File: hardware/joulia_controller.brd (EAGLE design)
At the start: 122.9 x 67.9 mm, 41 parts, among them IC1 LM2902D, IC2 LM2902D, U1 MMBT2222ALT1G, U2 MMBT2222ALT1G

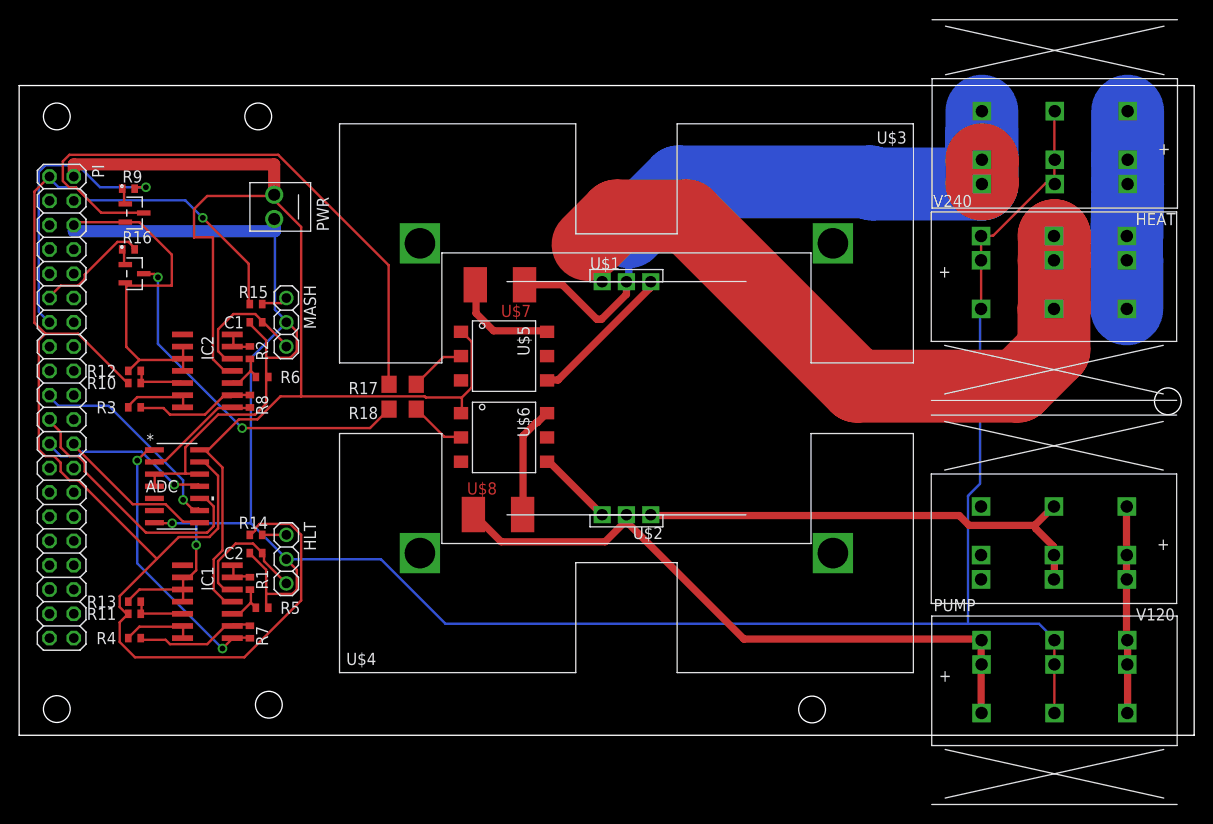
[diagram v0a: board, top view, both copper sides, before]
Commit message: Complete wiring with HV circuit and rearrangement
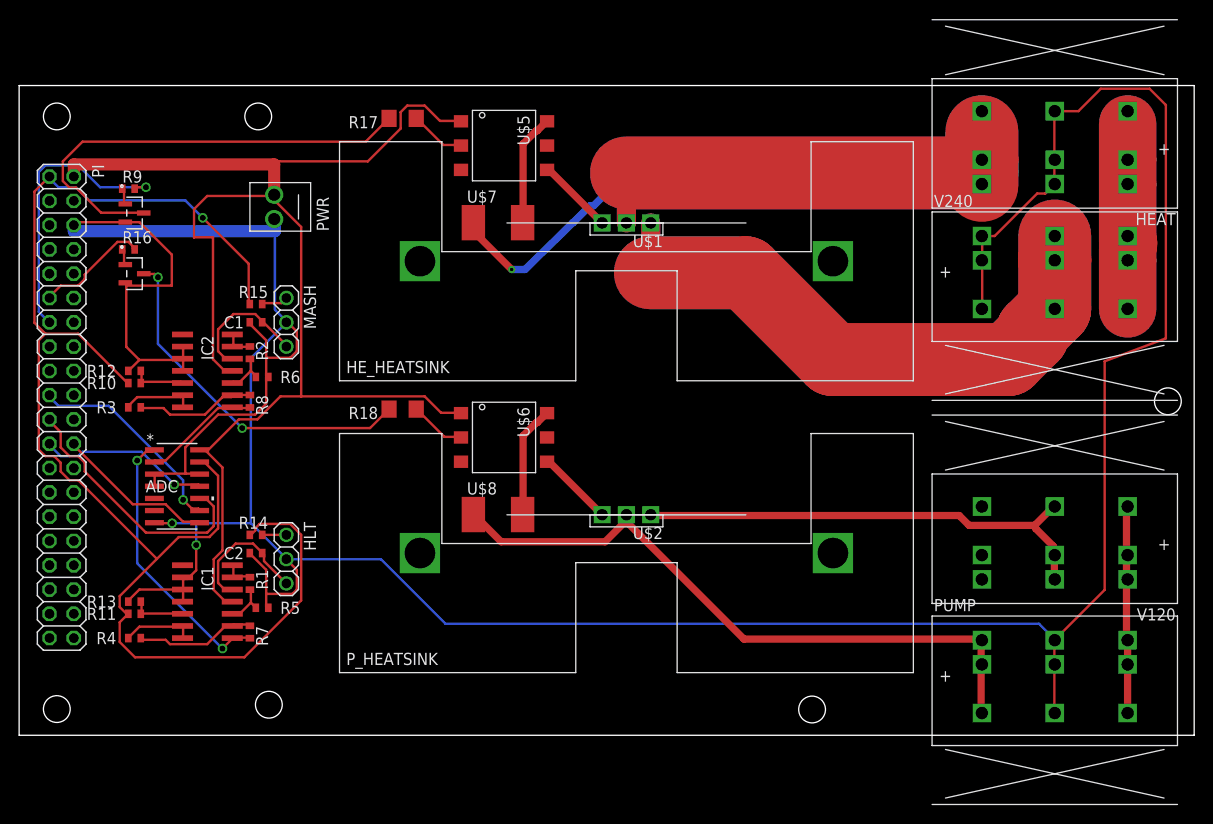
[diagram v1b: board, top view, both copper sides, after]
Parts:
- removed U$3: VM1-038-1AE, digikey:VM1-038-1AE
- added HE_HEATSINK: VM1-038-1AE, digikey:VM1-038-1AE
- moved R17 27.8 mm to (40.1, 64.5)
- moved U$5 22.0 mm to (50.7, 61.7)
- moved U$7 6.49 mm to (50.1, 53.6), turned to 0 degrees
- moved U$1 6.15 mm to (63.5, 53.6), turned to 180 degrees
- moved V120 0.08 mm to (108.3, 16.3)
- moved V240 0.08 mm to (108.3, 52.2)
- renumbered U$4 to P_HEATSINK
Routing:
- net N$22: track 74.7 -> 125.6 mm, vias 0 -> 1
- net N$32: track 75.5 -> 122.9 mm
- net GND: track 325.1 -> 367.4 mm
- net N$29: track 20.8 -> 43.8 mm
- net N$13: track 63.5 -> 47.9 mm
- net +5V: track 135.2 -> 150.0 mm
- net N$19: track 15.5 -> 8.06 mm

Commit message: Fix board size and hole placement.
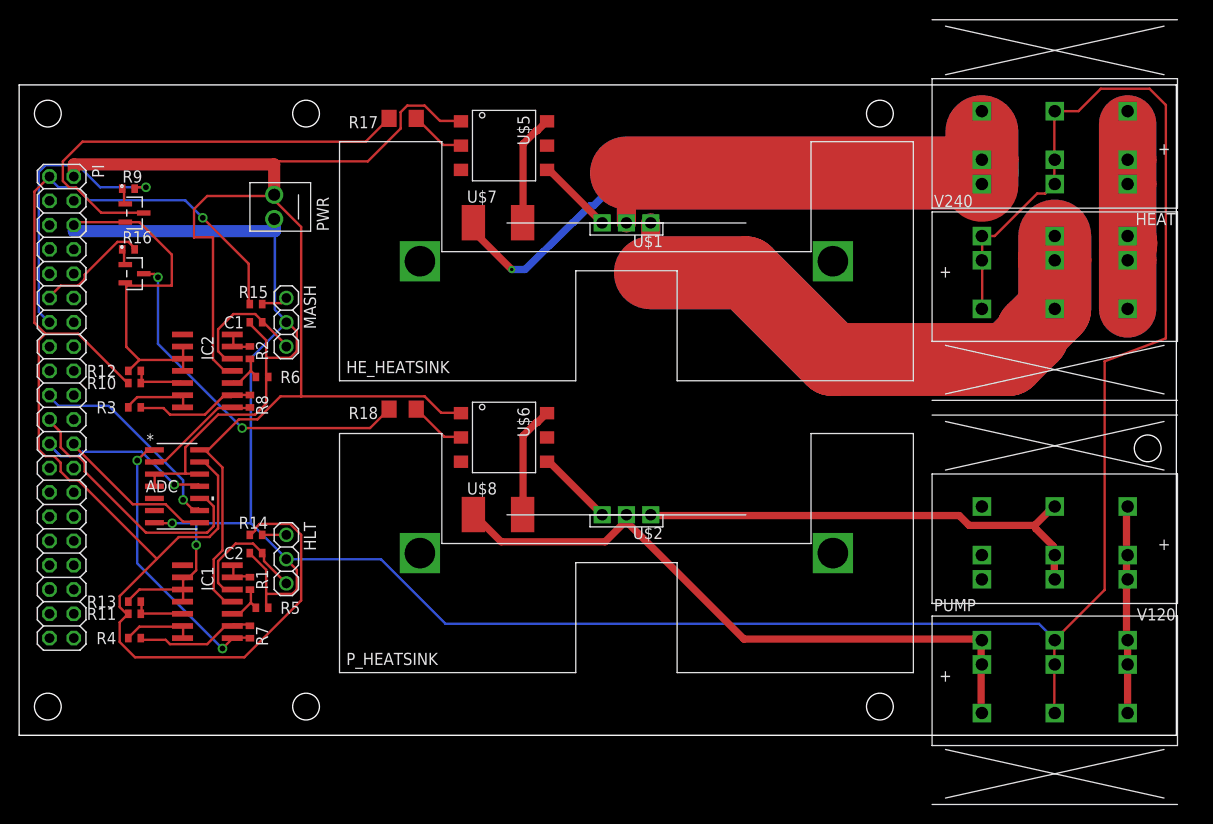
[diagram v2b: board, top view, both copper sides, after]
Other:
- board size 122.9 x 67.9 mm -> 121 x 68 mm
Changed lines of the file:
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@@
 <board>
 <plain>
-<wire x1="0" y1="0" x2="122.86" y2="0" width="0" layer="20"/>
-<wire x1="122.86" y1="0" x2="122.86" y2="67.935" width="0" layer="20"/>
-<wire x1="122.86" y1="67.935" x2="0" y2="67.935" width="0" layer="20"/>
-<wire x1="0" y1="67.935" x2="0" y2="0" width="0" layer="20"/>
-<hole x="3.94" y="64.705" drill="2.8"/>
-<hole x="82.91" y="2.695" drill="2.8"/>
-<hole x="3.94" y="2.74" drill="2.8"/>
-<hole x="120.11" y="34.92" drill="2.8"/>
+<wire x1="0" y1="0" x2="121" y2="0" width="0" layer="20"/>
+<wire x1="121" y1="0" x2="121" y2="68" width="0" layer="20"/>
+<wire x1="121" y1="68" x2="0" y2="68" width="0" layer="20"/>
+<wire x1="0" y1="68" x2="0" y2="0" width="0" layer="20"/>
+<hole x="3" y="65" drill="2.8"/>
+<hole x="90" y="3" drill="2.8"/>
+<hole x="3" y="3" drill="2.8"/>
+<hole x="118" y="30" drill="2.8"/>
 <text x="28.575" y="9.525" size="1.778" layer="26" rot="MR90">JOULIA HOMEBREW CONTROLLER</text>
 <text x="19.05" y="9.525" size="1.778" layer="26" rot="MR90">WILLIAM SCHMITT
 COPYRIGHT, 2017</text>
-<hole x="25" y="64.705" drill="2.8"/>
-<hole x="26.11" y="3.195" drill="2.8"/>
+<hole x="30" y="65" drill="2.8"/>
+<hole x="30" y="3" drill="2.8"/>
+<hole x="90" y="65" drill="2.8"/>
 </plain>
 <attributes>

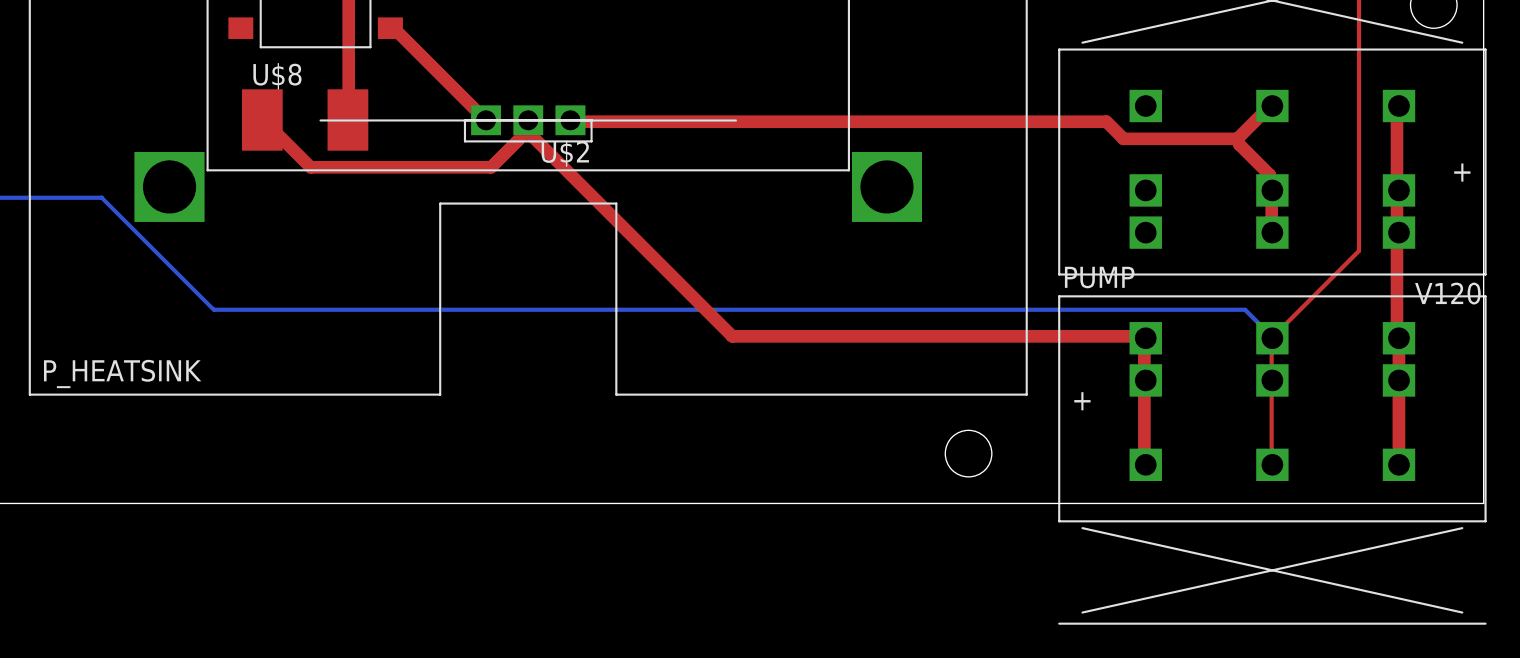
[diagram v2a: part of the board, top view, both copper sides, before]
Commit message: Adjust plugs to be consistently spaced.
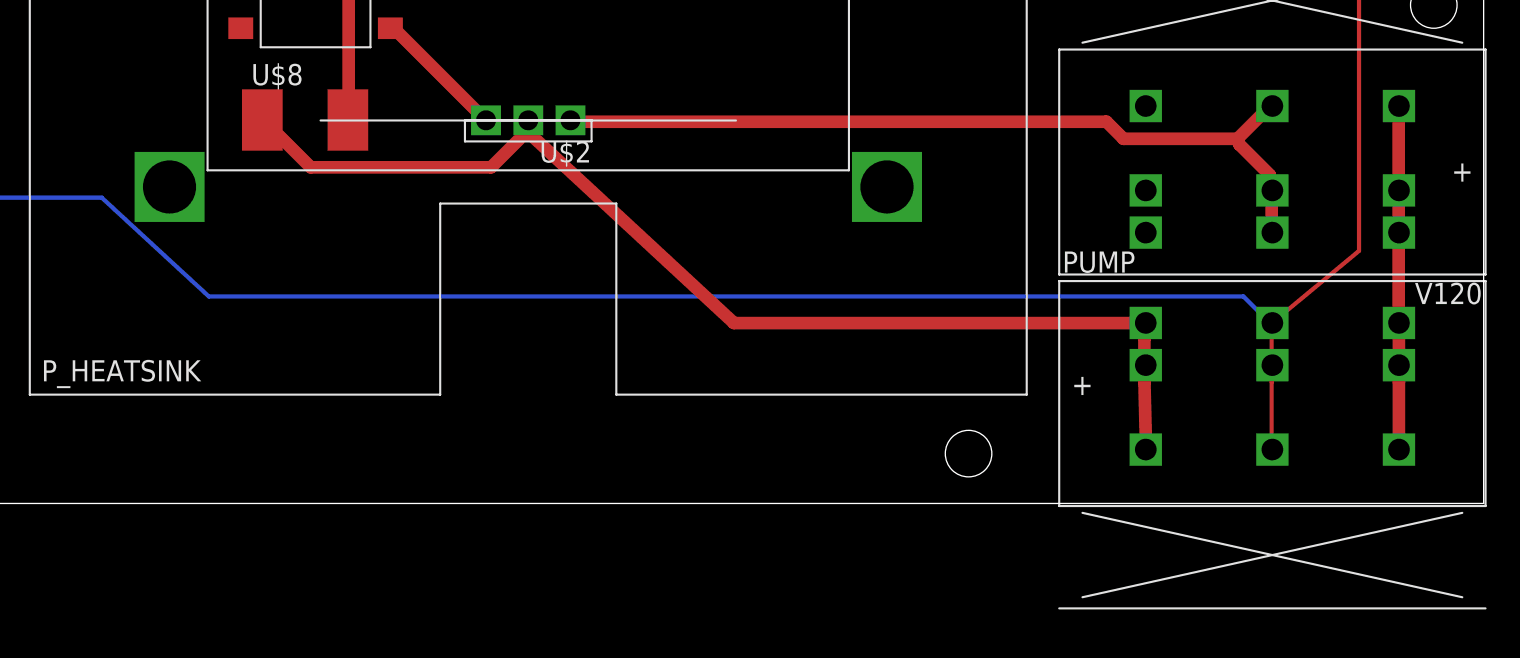
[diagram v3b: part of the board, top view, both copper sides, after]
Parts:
- moved PUMP 0.92 mm to (108.3, 10.9)
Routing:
- net N$27: track 21.9 -> 23.1 mm
- net GND: track 367.4 -> 368.1 mm
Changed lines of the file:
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@@
 <element name="U$8" library="digikey" package="2512(6432METRIC)" value="CRM2512" x="50.07" y="23.08"/>
 <element name="HEAT" library="digikey" package="PC-PCV5/3-G-7.62" value="PC1720589" x="108.285" y="57.635" rot="R180"/>
-<element name="PUMP" library="digikey" package="PC-PCV5/3-G-7.62" value="PC1720589" x="108.285" y="9.945"/>
+<element name="PUMP" library="digikey" package="PC-PCV5/3-G-7.62" value="PC1720589" x="108.285" y="10.865"/>
 <element name="V240" library="digikey" package="PC-PCV5/3-G-7.62" value="PC1720589" x="108.285" y="52.2"/>
 <element name="V120" library="digikey" package="PC-PCV5/3-G-7.62" value="PC1720589" x="108.285" y="16.3" rot="R180"/>
@@
 <wire x1="108.2421" y1="65.151" x2="108.285" y2="65.255" width="0.254" layer="1"/>
 <wire x1="108.2421" y1="60.2361" x2="108.285" y2="60.175" width="0.254" layer="1"/>
-<wire x1="108.2421" y1="7.3152" x2="108.2421" y2="2.4003" width="0.254" layer="1"/>
-<wire x1="108.2421" y1="2.4003" x2="108.285" y2="2.325" width="0.254" layer="1"/>
-<wire x1="108.2421" y1="7.3152" x2="108.285" y2="7.405" width="0.254" layer="1"/>
-<wire x1="108.2421" y1="9.9441" x2="108.2421" y2="7.4295" width="0.254" layer="1"/>
-<wire x1="108.2421" y1="9.9441" x2="108.285" y2="9.945" width="0.254" layer="1"/>
-<wire x1="108.2421" y1="7.4295" x2="108.285" y2="7.405" width="0.254" layer="1"/>
+<wire x1="108.2421" y1="7.3152" x2="108.2421" y2="3.3003" width="0.254" layer="1"/>
+<wire x1="108.2421" y1="3.3003" x2="108.285" y2="3.245" width="0.254" layer="1"/>
+<wire x1="108.2421" y1="7.3152" x2="108.285" y2="8.325" width="0.254" layer="1"/>
+<wire x1="108.2421" y1="10.8441" x2="108.2421" y2="7.4295" width="0.254" layer="1"/>
+<wire x1="108.2421" y1="10.8441" x2="108.285" y2="10.865" width="0.254" layer="1"/>
+<wire x1="108.2421" y1="7.4295" x2="108.285" y2="8.325" width="0.254" layer="1"/>
 <wire x1="37.8333" y1="18.4023" x2="28.0035" y2="18.4023" width="0.254" layer="16"/>
-<wire x1="44.577" y1="11.6586" x2="37.8333" y2="18.4023" width="0.254" layer="16"/>
-<wire x1="106.6419" y1="11.6586" x2="44.577" y2="11.6586" width="0.254" layer="16"/>
-<wire x1="108.2421" y1="10.0584" x2="106.6419" y2="11.6586" width="0.254" layer="16"/>
+<wire x1="44.277" y1="12.4586" x2="37.8333" y2="18.4023" width="0.254" layer="16"/>
+<wire x1="106.5419" y1="12.4586" x2="44.277" y2="12.4586" width="0.254" layer="16"/>
+<wire x1="108.2421" y1="10.7584" x2="106.5419" y2="12.4586" width="0.254" layer="16"/>
 <wire x1="28.0035" y1="18.4023" x2="27.94" y2="18.415" width="0.254" layer="16"/>
-<wire x1="108.2421" y1="10.0584" x2="108.285" y2="9.945" width="0.254" layer="16"/>
+<wire x1="108.2421" y1="10.7584" x2="108.285" y2="10.865" width="0.254" layer="16"/>
 <via x="16.002" y="22.1742" extent="1-16" drill="0.6096"/>
 <via x="18.5166" y="19.8882" extent="1-16" drill="0.6096"/>
@@
 <wire x1="119.9" y1="41.5" x2="113.5" y2="39.1" width="0.254" layer="1"/>
 <wire x1="113.5" y1="39.1" x2="113.5" y2="15.202" width="0.254" layer="1"/>
-<wire x1="113.5" y1="15.202" x2="108.2421" y2="9.9441" width="0.254" layer="1"/>
+<wire x1="113.5" y1="15.202" x2="108.2421" y2="10.8441" width="0.254" layer="1"/>
 </signal>
 <signal name="N$4">
@@
 <contactref element="PUMP" pad="P$7"/>
 <contactref element="PUMP" pad="P$9"/>
-<wire x1="100.584" y1="7.3152" x2="100.584" y2="2.4003" width="0.762" layer="1"/>
-<wire x1="100.584" y1="2.4003" x2="100.665" y2="2.325" width="0.762" layer="1"/>
-<wire x1="100.584" y1="7.3152" x2="100.665" y2="7.405" width="0.762" layer="1"/>
+<wire x1="100.584" y1="7.3152" x2="100.684" y2="3.2003" width="0.762" layer="1"/>
+<wire x1="100.684" y1="3.2003" x2="100.665" y2="3.245" width="0.762" layer="1"/>
+<wire x1="100.584" y1="7.3152" x2="100.665" y2="8.325" width="0.762" layer="1"/>
 <wire x1="100.584" y1="7.7724" x2="100.584" y2="9.9441" width="0.762" layer="1"/>
-<wire x1="100.584" y1="9.9441" x2="100.665" y2="9.945" width="0.762" layer="1"/>
-<wire x1="100.584" y1="7.7724" x2="100.665" y2="7.405" width="0.762" layer="1"/>
+<wire x1="100.584" y1="9.9441" x2="100.665" y2="10.865" width="0.762" layer="1"/>
+<wire x1="100.584" y1="7.7724" x2="100.665" y2="8.325" width="0.762" layer="1"/>
 <wire x1="63.4365" y1="22.4028" x2="63.4365" y2="22.9743" width="0.762" layer="1"/>
 <wire x1="61.2648" y1="20.2311" x2="63.4365" y2="22.4028" width="0.762" layer="1"/>
@@
 <wire x1="63.4365" y1="22.9743" x2="63.5" y2="23.06" width="0.762" layer="1"/>
 <wire x1="47.6631" y1="22.9743" x2="47.495" y2="23.08" width="0.762" layer="1"/>
-<wire x1="75.7809" y1="10.0584" x2="100.2411" y2="10.0584" width="0.762" layer="1"/>
-<wire x1="63.6651" y1="22.1742" x2="75.7809" y2="10.0584" width="0.762" layer="1"/>
-<wire x1="100.2411" y1="10.0584" x2="100.665" y2="9.945" width="0.762" layer="1"/>
+<wire x1="75.8809" y1="10.8584" x2="100.6411" y2="10.8584" width="0.762" layer="1"/>
+<wire x1="63.6651" y1="22.1742" x2="75.8809" y2="10.8584" width="0.762" layer="1"/>
+<wire x1="100.6411" y1="10.8584" x2="100.665" y2="10.865" width="0.762" layer="1"/>
 <wire x1="63.6651" y1="22.1742" x2="63.5" y2="23.06" width="0.762" layer="1"/>
 </signal>
@@
 <contactref element="V120" pad="P$9"/>
 <contactref element="V120" pad="P$8"/>
-<wire x1="115.7859" y1="18.7452" x2="115.7859" y2="16.3449" width="0.762" layer="1"/>
-<wire x1="115.7859" y1="16.3449" x2="115.905" y2="16.3" width="0.762" layer="1"/>
-<wire x1="115.7859" y1="18.7452" x2="115.905" y2="18.84" width="0.762" layer="1"/>
-<wire x1="115.7859" y1="19.2024" x2="115.7859" y2="23.8887" width="0.762" layer="1"/>
-<wire x1="115.7859" y1="23.8887" x2="115.905" y2="23.92" width="0.762" layer="1"/>
-<wire x1="115.7859" y1="19.2024" x2="115.905" y2="18.84" width="0.762" layer="1"/>
-<wire x1="115.9002" y1="7.3152" x2="115.9002" y2="2.4003" width="0.762" layer="1"/>
-<wire x1="115.9002" y1="2.4003" x2="115.905" y2="2.325" width="0.762" layer="1"/>
-<wire x1="115.9002" y1="7.3152" x2="115.905" y2="7.405" width="0.762" layer="1"/>
+<wire x1="115.8859" y1="18.7452" x2="115.8859" y2="16.3449" width="0.762" layer="1"/>
+<wire x1="115.8859" y1="16.3449" x2="115.905" y2="16.3" width="0.762" layer="1"/>
+<wire x1="115.8859" y1="18.7452" x2="115.905" y2="18.84" width="0.762" layer="1"/>
+<wire x1="115.8859" y1="19.2024" x2="115.8859" y2="23.8887" width="0.762" layer="1"/>
+<wire x1="115.8859" y1="23.8887" x2="115.905" y2="23.92" width="0.762" layer="1"/>
+<wire x1="115.8859" y1="19.2024" x2="115.905" y2="18.84" width="0.762" layer="1"/>
+<wire x1="115.9002" y1="7.3152" x2="115.9002" y2="3.2003" width="0.762" layer="1"/>
+<wire x1="115.9002" y1="3.2003" x2="115.905" y2="3.245" width="0.762" layer="1"/>
+<wire x1="115.9002" y1="7.3152" x2="115.905" y2="8.325" width="0.762" layer="1"/>
 <wire x1="115.9002" y1="7.7724" x2="115.9002" y2="9.9441" width="0.762" layer="1"/>
-<wire x1="115.9002" y1="9.9441" x2="115.905" y2="9.945" width="0.762" layer="1"/>
-<wire x1="115.9002" y1="7.7724" x2="115.905" y2="7.405" width="0.762" layer="1"/>
-<wire x1="115.7859" y1="10.287" x2="115.7859" y2="16.002" width="0.762" layer="1"/>
-<wire x1="115.7859" y1="16.002" x2="115.905" y2="16.3" width="0.762" layer="1"/>
-<wire x1="115.7859" y1="10.287" x2="115.905" y2="9.945" width="0.762" layer="1"/>
+<wire x1="115.9002" y1="9.9441" x2="115.905" y2="10.865" width="0.762" layer="1"/>
+<wire x1="115.9002" y1="7.7724" x2="115.905" y2="8.325" width="0.762" layer="1"/>
+<wire x1="115.8859" y1="10.287" x2="115.8859" y2="16.302" width="0.762" layer="1"/>
+<wire x1="115.8859" y1="16.302" x2="115.905" y2="16.3" width="0.762" layer="1"/>
+<wire x1="115.8859" y1="10.287" x2="115.905" y2="10.865" width="0.762" layer="1"/>
 </signal>
 <signal name="N$29" class="2">
